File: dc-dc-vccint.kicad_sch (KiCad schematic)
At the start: 57 parts, among them U36 MP8796B, U4 MP8796B

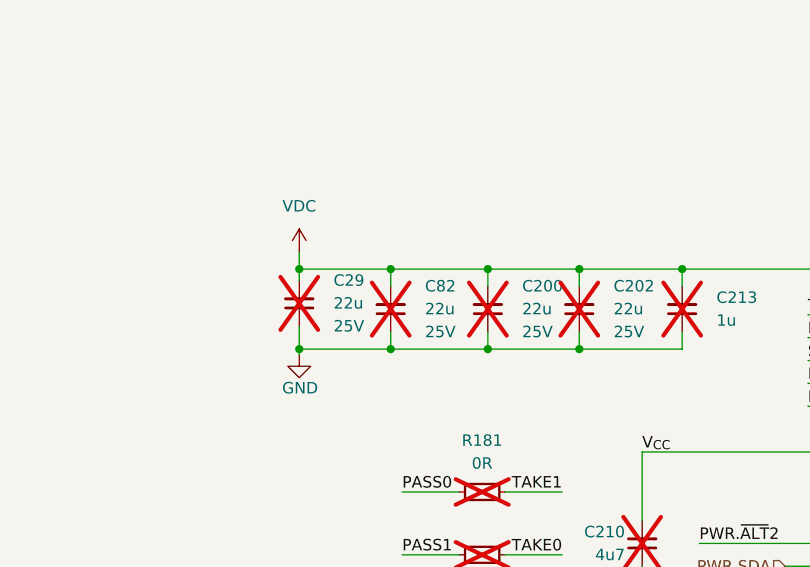
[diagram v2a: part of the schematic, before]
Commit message: [#66727] Fix schematic errors
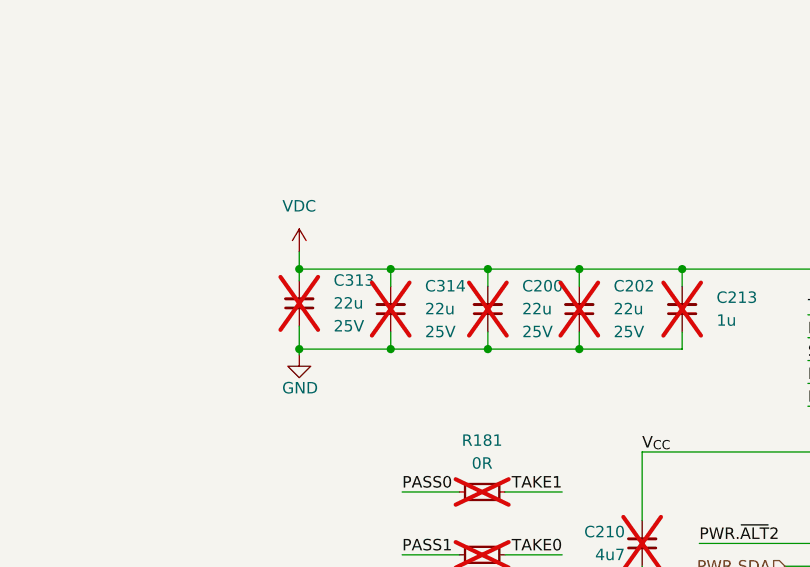
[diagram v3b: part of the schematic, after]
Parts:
- renumbered C29 to C313, C82 to C314
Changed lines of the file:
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@@
   (symbol (lib_name "C_22u_25V_0805_1") (lib_id "antmicroCapacitorsmisc:C_22u_25V_0805") (at 114.935 158.75 90) (unit 1)
     (in_bom no) (on_board yes) (dnp yes) (fields_autoplaced)
-    (property "Reference" "C29" (at 118.745 153.6636 90)
+    (property "Reference" "C313" (at 118.745 153.6636 90)
       (effects (font (size 1.27 1.27) (thickness 0.15)) (justify right))
     )
@@
       (project "data-center-rdimm-ddr5-tester"
         (path "/1faa6543-e26a-4449-8bac-ee14b9f19e5f/00000000-0000-0000-0000-000060225b0c/3cfc3a6a-24b0-4207-8c35-05eeccc29696"
-          (reference "C29") (unit 1)
+          (reference "C313") (unit 1)
         )
       )
@@
   (symbol (lib_name "C_22u_25V_0805_1") (lib_id "antmicroCapacitorsmisc:C_22u_25V_0805") (at 125.095 159.385 90) (unit 1)
     (in_bom no) (on_board yes) (dnp yes) (fields_autoplaced)
-    (property "Reference" "C82" (at 128.905 154.2986 90)
+    (property "Reference" "C314" (at 128.905 154.2986 90)
       (effects (font (size 1.27 1.27) (thickness 0.15)) (justify right))
     )
@@
       (project "data-center-rdimm-ddr5-tester"
         (path "/1faa6543-e26a-4449-8bac-ee14b9f19e5f/00000000-0000-0000-0000-000060225b0c/3cfc3a6a-24b0-4207-8c35-05eeccc29696"
-          (reference "C82") (unit 1)
-        )
-      )
+          (reference "C314") (unit 1)
+        )
+      )

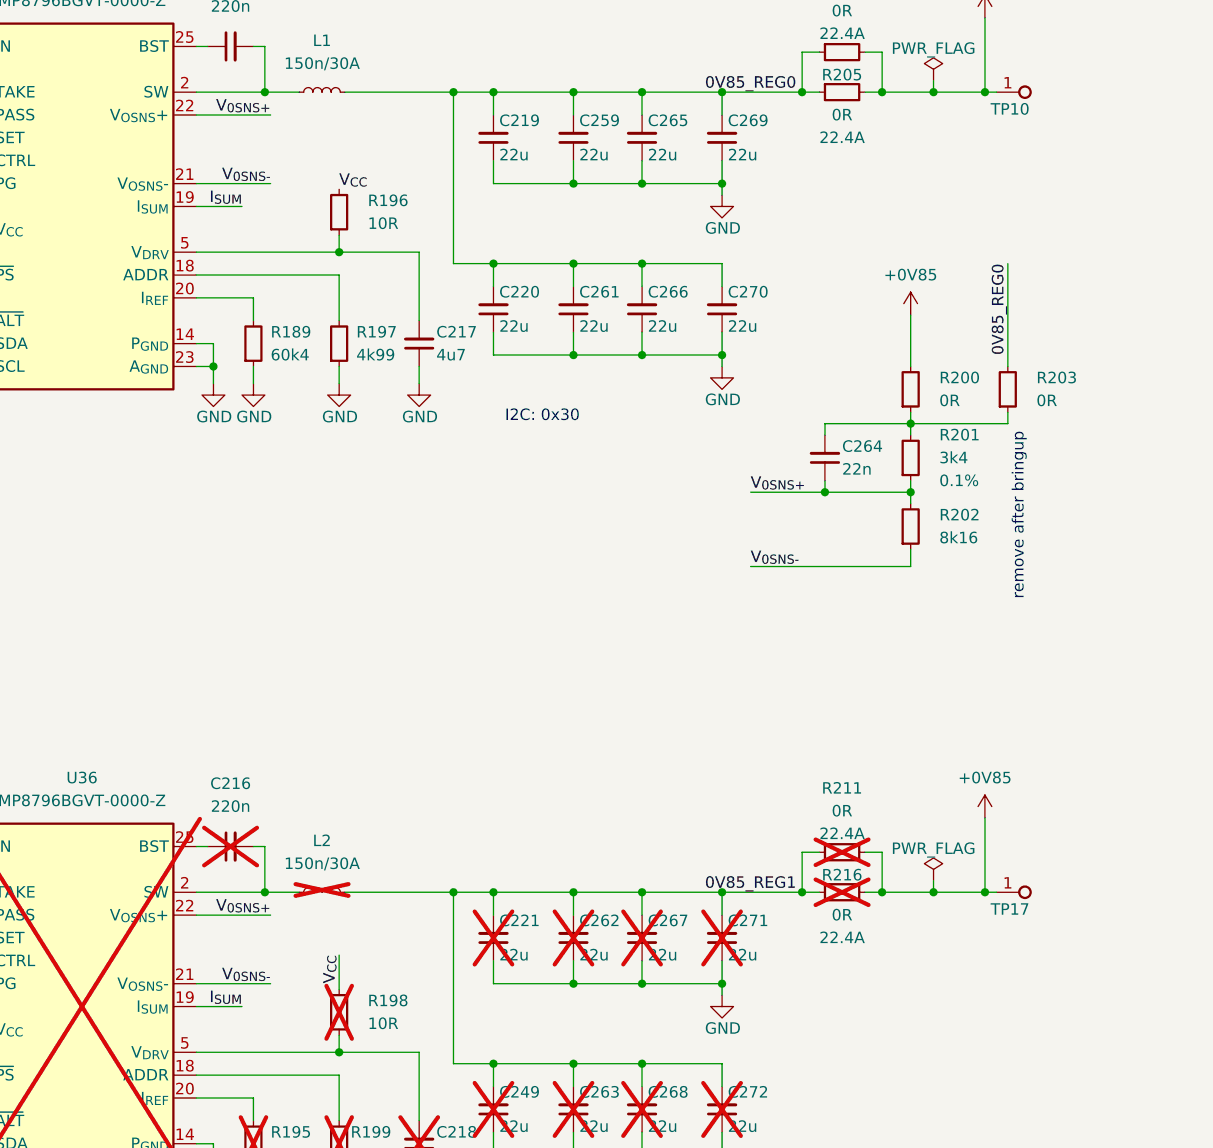
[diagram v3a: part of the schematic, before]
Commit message: [#66727] Route VCCINT sense. Route VREF. Place supply power meters circuits
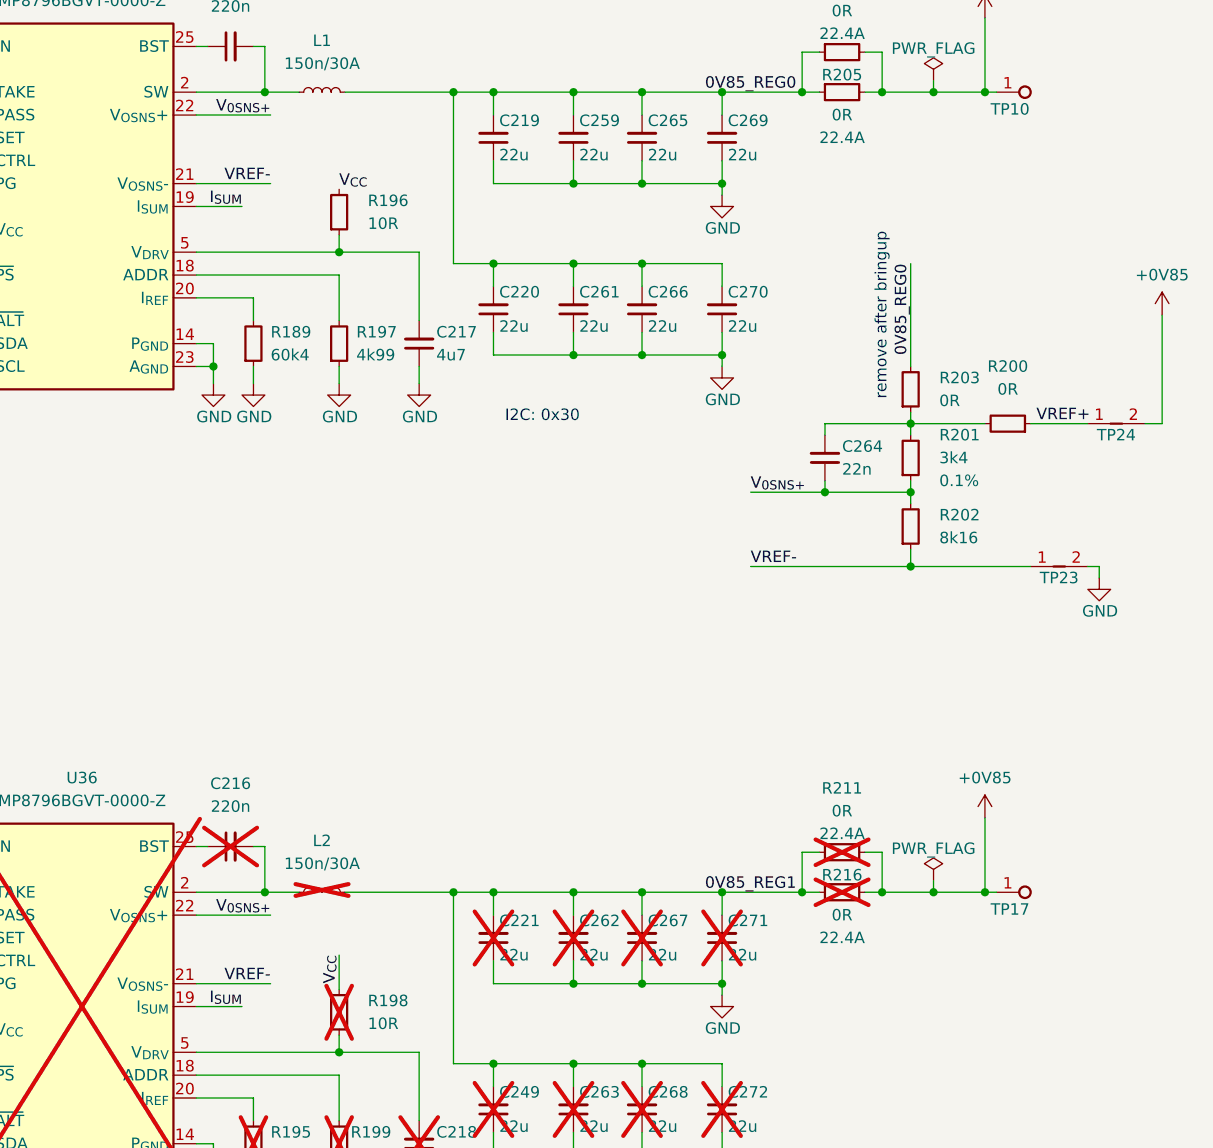
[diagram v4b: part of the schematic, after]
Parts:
- added TP23, TP24: Net-Tie_P0.127mm, antmicro-footprints:NetTie-2_SMD_Pad0.127mm, symbol ShuntsJumpers:Net-Tie_P0.127mm
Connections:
- net +0V85: now also TP24.2; no longer R200.2
- net GND: now also TP23.2
- net at C264.2, R201.2, R203.1: now also R200.2; no longer R200.1
- net V_{0SNS-} renamed VREF-
- net VREF-: now also TP23.1
- new net VREF+: R200.1, TP24.1
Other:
- moved on the sheet: R200, R203

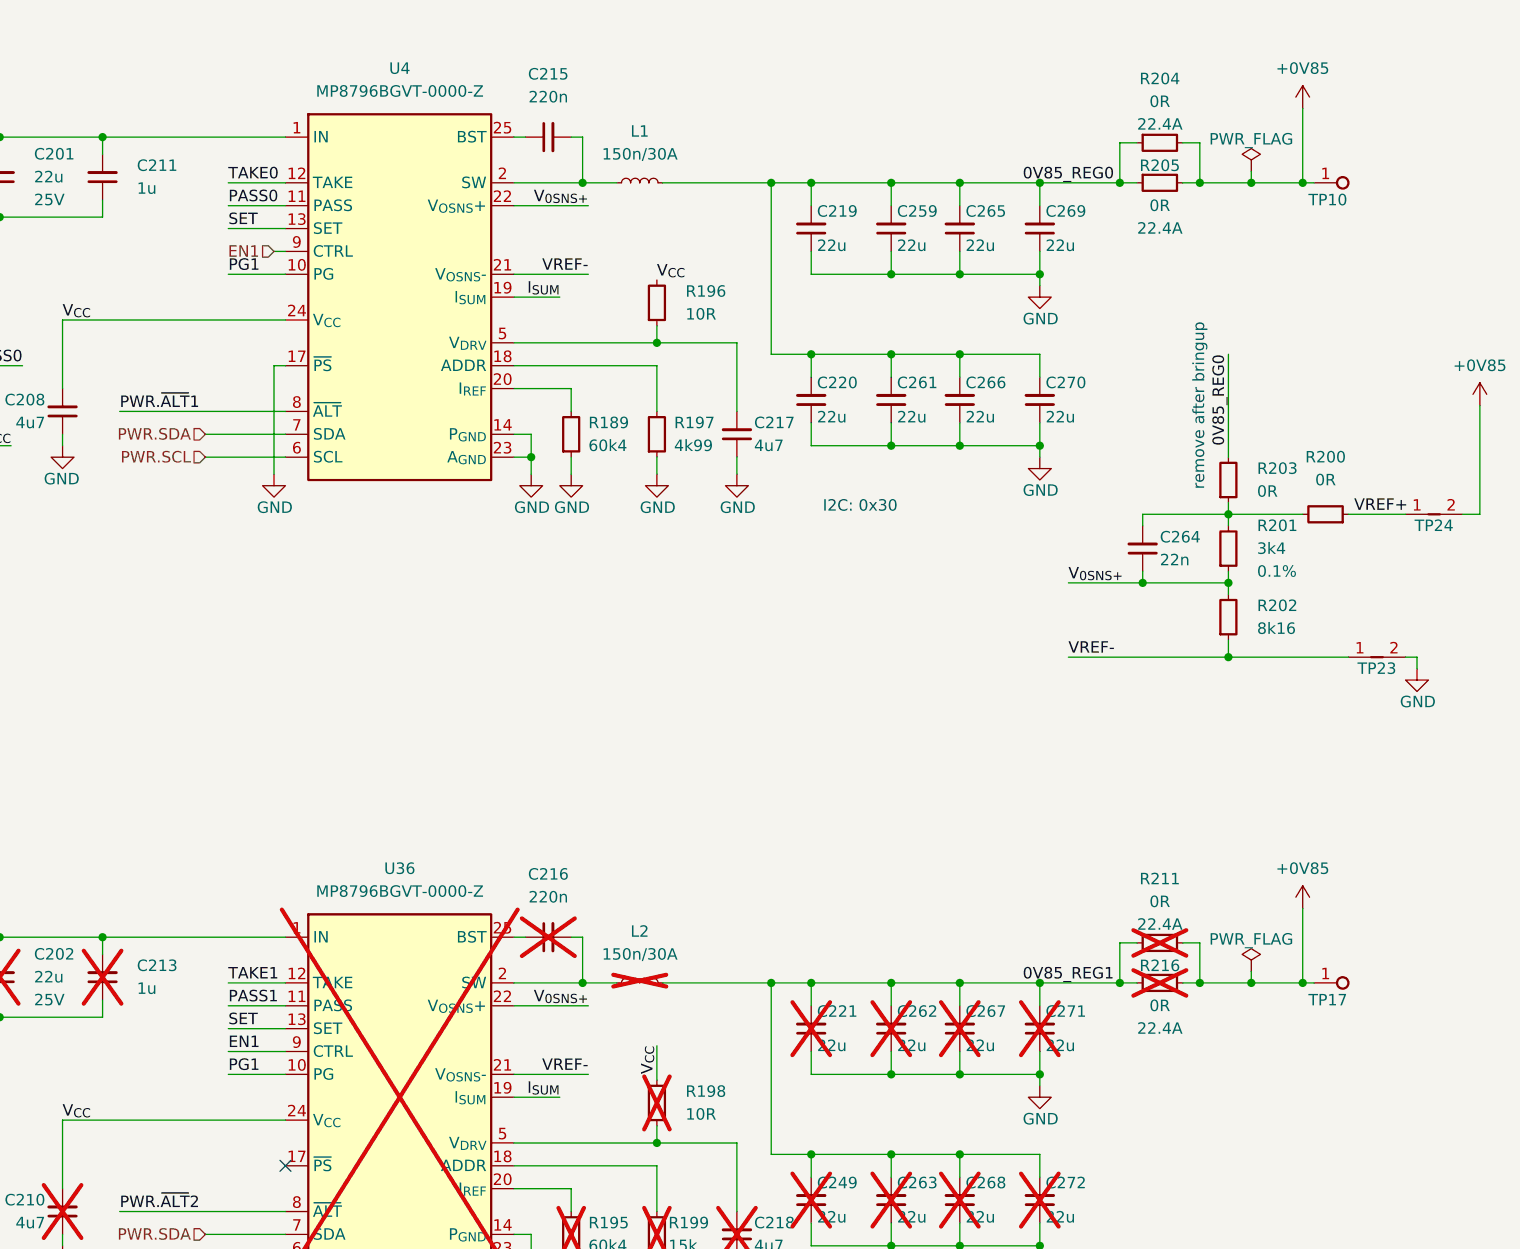
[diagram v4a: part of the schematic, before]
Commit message: [#66727] Continue routing low speed signals
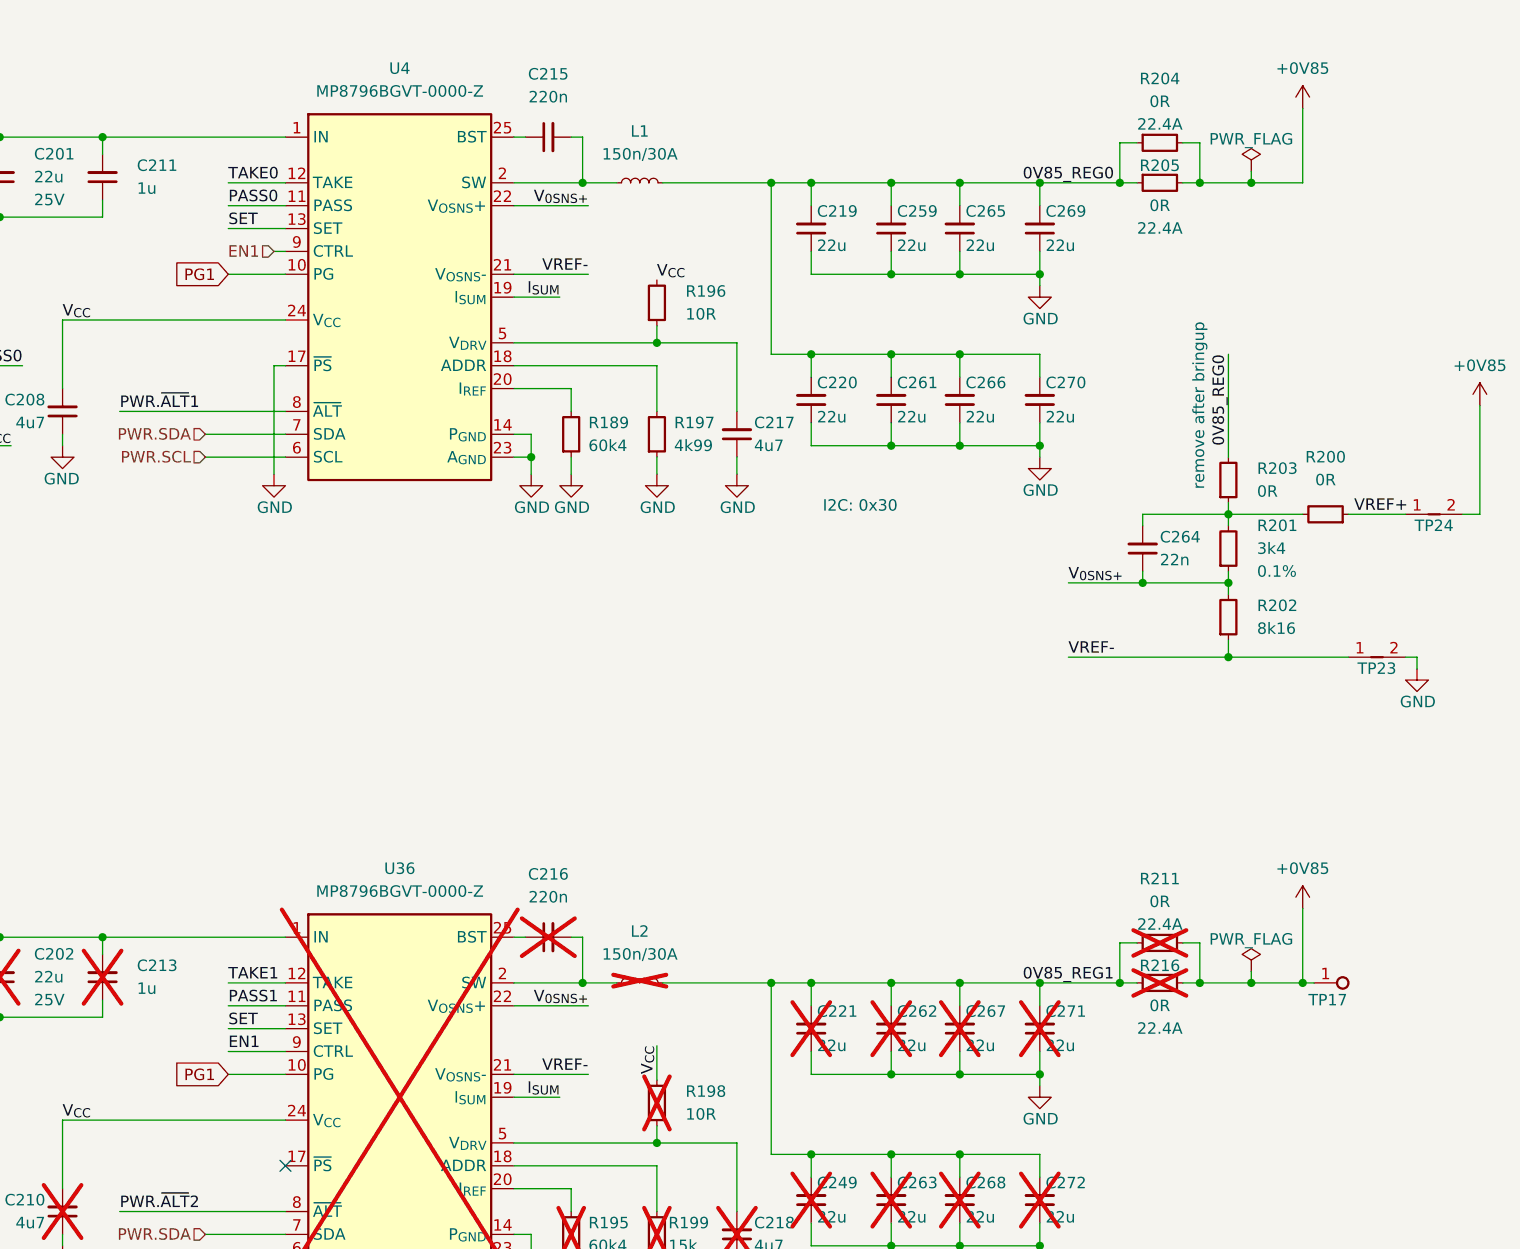
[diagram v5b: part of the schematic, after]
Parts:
- removed TP10: TP_1mm_SMD, antmicro-footprints:TP_SMD_1mm, symbol antmicroTestPoints:TP_1mm_SMD
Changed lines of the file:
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@@
   (junction (at 252.73 157.48) (diameter 0) (color 0 0 0 0)
-  )
-  (junction (at 290.83 68.58) (diameter 0) (color 0 0 0 0)
   )
   (junction (at 261.62 186.69) (diameter 0) (color 0 0 0 0)
@@
     (stroke (width 0) (type default))
   )
-  (wire (pts (xy 290.83 68.58) (xy 292.1 68.58))
-    (stroke (width 0) (type default))
-  )
   (wire (pts (xy 279.4 157.48) (xy 285.115 157.48))
     (stroke (width 0) (type default))
@@
     (effects (font (size 1.27 1.27)) (justify right bottom))
   )
-  (label "PG1" (at 171.45 167.64 0) (fields_autoplaced)
-    (effects (font (size 1.27 1.27)) (justify left bottom))
-  )
   (label "SET" (at 171.45 162.56 0) (fields_autoplaced)
     (effects (font (size 1.27 1.27)) (justify left bottom))
@@
     (effects (font (size 1.27 1.27)) (justify left bottom))
   )
-  (label "PG1" (at 171.45 78.74 0) (fields_autoplaced)
-    (effects (font (size 1.27 1.27)) (justify left bottom))
-  )
   (label "I_{SUM}" (at 208.28 81.28 180) (fields_autoplaced)
     (effects (font (size 1.27 1.27)) (justify right bottom))
@@
   (label "0V85_REG0" (at 259.715 68.58 0) (fields_autoplaced)
     (effects (font (size 1.27 1.27)) (justify left bottom))
+  )
+  (global_label "PG1" (shape input) (at 171.45 78.74 180) (fields_autoplaced)
+    (effects (font (size 1.27 1.27)) (justify right))
+    (property "Intersheetrefs" "${INTERSHEET_REFS}" (at 165.3695 78.74 0)
+      (effects (font (size 1.27 1.27)) (justify right))
+    )
+  )
+  (global_label "PG1" (shape input) (at 171.45 167.64 180) (fields_autoplaced)
+    (effects (font (size 1.27 1.27)) (justify right))
+    (property "Intersheetrefs" "${INTERSHEET_REFS}" (at 165.3695 167.64 0)
+      (effects (font (size 1.27 1.27)) (justify right))
+    )
   )
   (hierarchical_label "PWR.SDA" (shape input) (at 168.91 96.52 180) (fields_autoplaced)
@@
         )
       )
-    )
-  )
-  (symbol (lib_id "antmicroTestPoints:TP_1mm_SMD") (at 292.1 68.58 0) (unit 1)
-    (in_bom yes) (on_board yes) (dnp no)
-    (property "Reference" "TP10" (at 291.465 70.485 0)
-      (effects (font (size 1.27 1.27)) (justify left))
-    )
-    (property "Value" "TP_1mm_SMD" (at 307.34 76.2 0)
-      (effects (font (size 1.27 1.27) (thickness 0.15)) (justify left bottom) hide)
-    )
-    (property "Footprint" "antmicro-footprints:TP_SMD_1mm" (at 307.34 78.74 0)
-      (effects (font (size 1.27 1.27) (thickness 0.15)) (justify left bottom) hide)
-    )
-    (property "Datasheet" "" (at 307.34 81.28 0)
-      (effects (font (size 1.27 1.27) (thickness 0.15)) (justify left bottom) hide)
-    )
-    (property "MPN" "" (at 292.1 68.58 0)
-      (effects (font (size 1.27 1.27)) hide)
-    )
-    (property "Manufacturer" "" (at 292.1 68.58 0)
-      (effects (font (size 1.27 1.27)) hide)
-    )
-    (property "Author" "Antmicro" (at 307.34 83.82 0)
-      (effects (font (size 1.27 1.27) (thickness 0.15)) (justify left bottom) hide)
-    )
-    (property "License" "Apache-2.0" (at 307.34 86.36 0)
-      (effects (font (size 1.27 1.27) (thickness 0.15)) (justify left bottom) hide)
-    )
-    (pin "1")
-    (instances
-      (project "data-center-rdimm-ddr5-tester"
-        (path "/1faa6543-e26a-4449-8bac-ee14b9f19e5f/00000000-0000-0000-0000-000060225b0c/3cfc3a6a-24b0-4207-8c35-05eeccc29696"
-          (reference "TP10") (unit 1)
-        )
-      )

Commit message: [#67725] Update vccint power supply
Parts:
- added TP10, TP25, TP26: TP_1mm_SMD, antmicro-footprints:TP_SMD_1mm, symbol antmicroTestPoints:TP_1mm_SMD
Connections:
- net PWR.~{ALT}1: now also TP10.1
- net PWR.~{ALT}2: now also TP25.1
- net ~{PS}: now reaches U36.17 (~{PS})
- net ~{PS}: now also TP26.1
- no-connect marks 1 -> 0
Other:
- moved on the sheet: C177, C200, C201, C202, C208, C21, C210, C211, C213, C215, C216, C217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
